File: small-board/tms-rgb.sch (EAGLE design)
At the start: 39 parts, among them J1 Pads, U1 CD74HC4053PWR, U100 TMS992XA, U2 TS5A4597DCKR, U3 LM1881MX/NOPB, U4 MAX4395EUD, U5 SN74LVC2G17DCKR, U6 LMH1251MT/NOPB, U7 THS7374IPWR

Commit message: Major layout rework for v2
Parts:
- removed C16: 100nF, tms-rgb:C0603
- C10: value 100nF -> 10uF; device tms-rgb:C0603 -> tms-rgb:C1206
- C11: value 10uF -> 100nF; device tms-rgb:C1206 -> tms-rgb:C0603
- R2: value 150 -> 910
- R3: value 220 -> 680
- R4: value 680 -> 220
- R6: value 910 -> 150
- U2: value TS5A4597DCKR -> LM1881MX/NOPB; device tms-rgb:TS5A4597DCKR -> tms-rgb:LM1881MX/NOPB
- U3: value LM1881MX/NOPB -> MAX4395EUD; device tms-rgb:LM1881MX/NOPB -> tms-rgb:MAX4395EUD
- U4: value MAX4395EUD -> TS5A4597DCKR; device tms-rgb:MAX4395EUD -> tms-rgb:TS5A4597DCKR
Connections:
- net B-Y: now also U1.Z1, U4.NC; no longer U1.Y1, U2.NC
- net CSYNC: now also U4.IN; no longer U2.IN
- net GND: now also C10.2, U3.VEE, U4.GND; no longer C16.2, C5.2, U3.GND, U4.VEE
- net N$1: now also R4.1, U3.A, U3.A-; no longer R3.1, U4.A, U4.A-
- net N$10: now also U1.Y, U3.C+; no longer U1.X, U4.C+
- net N$12: now also C9.1, R4.2, R7.2; no longer C7.1, R2.2, R3.2
- net N$13: now also C6.1, R2.2, R3.2; no longer C8.1, R4.2, R6.2
- net N$14: now also C5.1, C7.1, C8.1, R6.2; no longer C10.1, C6.1, C9.1, R7.2
- net N$2: now also R3.1, U3.B, U3.B-; no longer R4.1, U4.B, U4.B-
- net N$20: now also C5.2, U2.VIDEO_IN; no longer C6.2, U3.VIDEO_IN
- net N$21: now also C9.2; no longer C7.2
- net N$22: now also C6.2; no longer C8.2
- net N$23: now also C8.2; no longer C10.2
- net N$24: now also C7.2; no longer C9.2
- net N$3: now also U3.C, U3.C-; no longer U4.C, U4.C-
- net N$4: now also U3.D+, U4.COM; no longer U2.COM, U4.D+
- net N$5: now also U2.BURST; no longer U3.BURST
- net N$6: now also U2.CSYNC; no longer U3.CSYNC
- net N$7: now also U2.R_SET; no longer U3.R_SET
- net N$8: now also U1.X, U3.A+; no longer U1.Z, U4.A+
- net N$9: now also U1.Z, U3.B+; no longer U1.Y, U4.B+
- net R-Y: now also U1.X1; no longer U1.Z1
- net SAMPLE: now also U1.X0, U3.D, U3.D-; no longer U1.Y0, U4.D, U4.D-
- net VCC: now also C10.1; no longer C16.1, C5.1
- net Y: now also U1.Y0, U1.Y1; no longer U1.X0, U1.X1
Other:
- moved on the sheet: C1, C10, C11, C12, C13, C14, C15, C2, C3, C4, C5, C6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

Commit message: Named a few signals
And bridged a distant VCC fill
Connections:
- net N$10 renamed MX_Y
- net N$12 renamed SC_R
- net N$13 renamed SC_B
- net N$14 renamed SC_Y
- net N$4 renamed HOLD
- net N$8 renamed MX_R
- net N$9 renamed MX_B
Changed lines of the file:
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@@
 </segment>
 </net>
-<net name="N$8" class="0">
+<net name="MX_R" class="0">
 <segment>
 <pinref part="U1" gate="A" pin="X"/>
@@
 </segment>
 </net>
-<net name="N$9" class="0">
+<net name="MX_B" class="0">
 <segment>
 <pinref part="U1" gate="A" pin="Z"/>
@@
 </segment>
 </net>
-<net name="N$10" class="0">
+<net name="MX_Y" class="0">
 <segment>
 <pinref part="U1" gate="A" pin="Y"/>
@@
 </segment>
 </net>
-<net name="N$12" class="0">
+<net name="SC_R" class="0">
 <segment>
 <pinref part="R4" gate="G$1" pin="2"/>
@@
 </segment>
 </net>
-<net name="N$13" class="0">
+<net name="SC_B" class="0">
 <segment>
 <pinref part="R3" gate="G$1" pin="2"/>
@@
 </segment>
 </net>
-<net name="N$14" class="0">
+<net name="SC_Y" class="0">
 <segment>
 <pinref part="R5" gate="G$1" pin="2"/>
@@
 </segment>
 </net>
-<net name="N$4" class="0">
+<net name="HOLD" class="0">
 <segment>
 <pinref part="U3" gate="A" pin="D+"/>

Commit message: More than 100 improvements
Nearly all of which were suggested by MrPix from the AtariAge forums to improve the electrical characteristics of the board.
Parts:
- removed C15: 100nF, tms-rgb:C0603
- added FID1, FID2: FIDUCIAL, tms-rgb:FIDUCIAL
- C10: value 10uF -> 100nF; device tms-rgb:C1206 -> tms-rgb:C0603
- C3: value 100nF -> 10nF
- C4: value 10nF -> 100nF
- C9: value 100nF -> 10uF; device tms-rgb:C0603 -> tms-rgb:C1206
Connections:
- net GND: now also C14.2, C9.2; no longer C11.2, C15.2, C4.2
- net HOLD: now also C3.1; no longer C4.1
- net N$20: now also C4.2; no longer C5.2
- net N$21: now also C5.2; no longer C9.2
- net N$25: now also C11.1; no longer C12.1
- net N$26: now also C12.1; no longer C13.1
- net N$27: now also C13.1; no longer C14.1
- net N$28: now also C11.2; no longer C12.2
- net N$29: now also C12.2; no longer C13.2
- net N$30: now also C13.2; no longer C14.2
- net SC_R: now also C5.1, R6.2; no longer C9.1, R7.2
- net SC_Y: now also C4.1, R7.2; no longer C5.1, R6.2
- net VCC: now also C14.1, C9.1; no longer C11.1, C15.1, C3.1
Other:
- note added: "Nicholas Piegdon May 31, 2020 v2 CERN-OHL-W v2 github.com/npiegdon/tms-rgb nicholas.piegdon.info/tms-rgb @npiegdon"
- note removed: "Nicholas Piegdon May 17, 2020 v1+ CERN-OHL-W v2 github.com/npiegdon/tms-rgb nicholas.piegdon.info/tms-rgb @npiegdon"
- moved on the sheet: C10, C11, C12, C13, C14, C3, C4, C5, C9, R6, R7

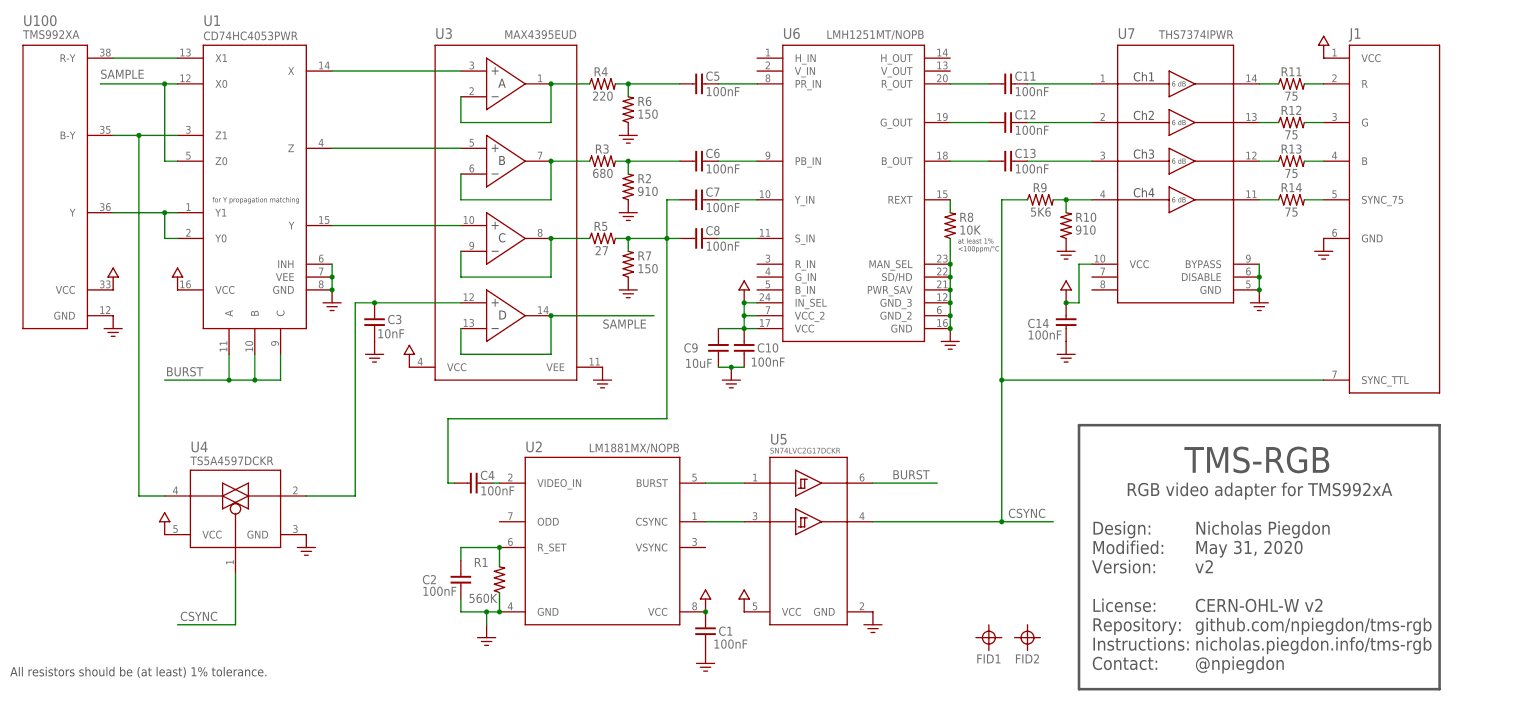
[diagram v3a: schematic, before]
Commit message: Updated voltage dividers
Now we consume around 15mA less with no discernible change to the image.
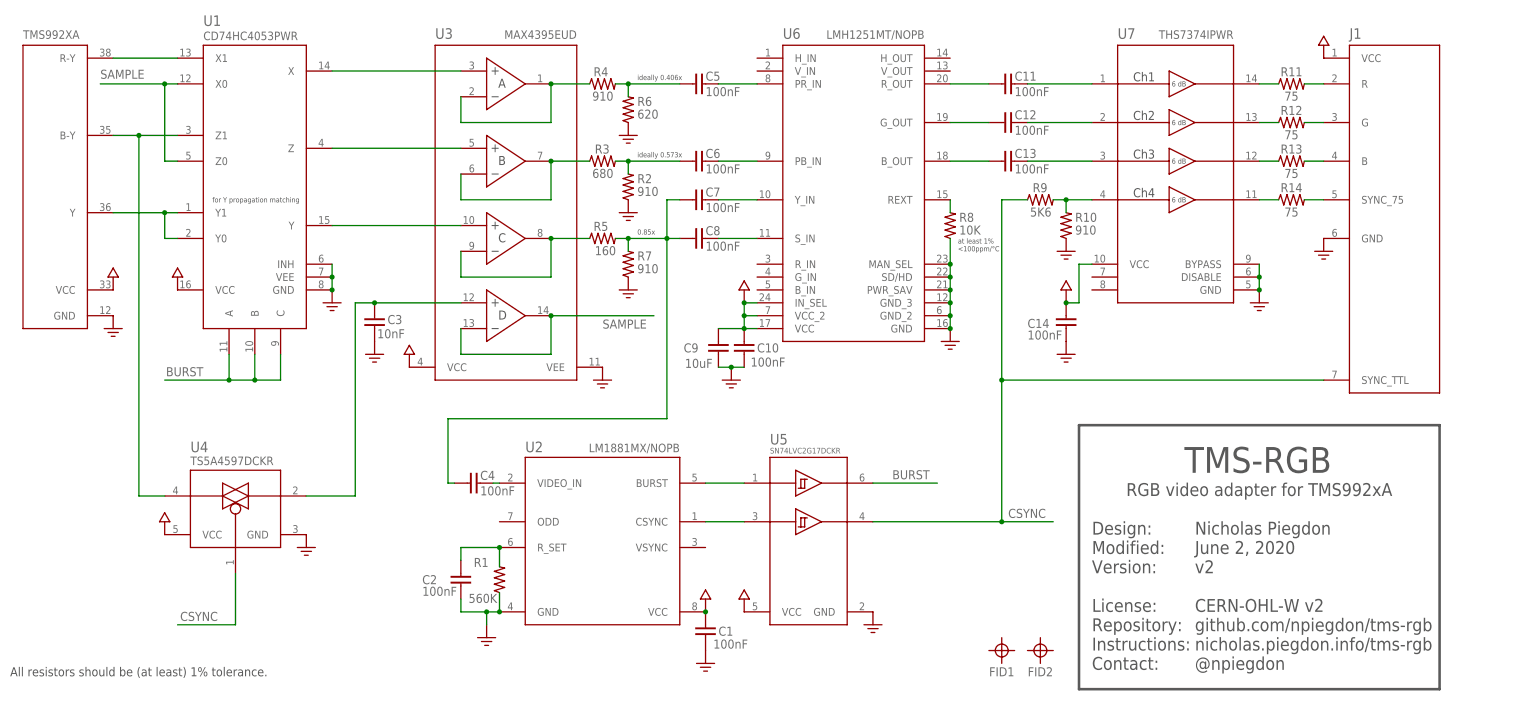
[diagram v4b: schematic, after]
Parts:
- R4: value 220 -> 910
- R5: value 27 -> 160
- R6: value 150 -> 620
- R7: value 150 -> 910
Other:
- note added: "0.85x"
- note added: "Nicholas Piegdon June 2, 2020 v2 CERN-OHL-W v2 github.com/npiegdon/tms-rgb nicholas.piegdon.info/tms-rgb @npiegdon"
- note added: "ideally 0.406x"
- note added: "ideally 0.573x"
- note removed: "Nicholas Piegdon May 31, 2020 v2 CERN-OHL-W v2 github.com/npiegdon/tms-rgb nicholas.piegdon.info/tms-rgb @npiegdon"
- moved on the sheet: FID1, FID2
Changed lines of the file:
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@@
 <part name="SUPPLY8" library="tms-rgb" deviceset="5V" device=""/>
 <part name="R8" library="tms-rgb" deviceset="R" device="0603" value="10K"/>
-<part name="R4" library="tms-rgb" deviceset="R" device="0603" value="220"/>
+<part name="R4" library="tms-rgb" deviceset="R" device="0603" value="910"/>
 <part name="R3" library="tms-rgb" deviceset="R" device="0603" value="680"/>
-<part name="R5" library="tms-rgb" deviceset="R" device="0603" value="27"/>
-<part name="R6" library="tms-rgb" deviceset="R" device="0603" value="150"/>
+<part name="R5" library="tms-rgb" deviceset="R" device="0603" value="160"/>
+<part name="R6" library="tms-rgb" deviceset="R" device="0603" value="620"/>
 <part name="R2" library="tms-rgb" deviceset="R" device="0603" value="910"/>
-<part name="R7" library="tms-rgb" deviceset="R" device="0603" value="150"/>
+<part name="R7" library="tms-rgb" deviceset="R" device="0603" value="910"/>
 <part name="GND9" library="tms-rgb" deviceset="GND" device=""/>
 <part name="GND10" library="tms-rgb" deviceset="GND" device=""/>
@@
 <plain>
 <text x="236.22" y="33.02" size="2.54" layer="97" align="top-left">Nicholas Piegdon
-May 31, 2020
+June 2, 2020
 v2
 CERN-OHL-W v2
@@
 <text x="2.54" y="2.54" size="1.778" layer="97">All resistors should be (at least) 1% tolerance.</text>
 <text x="42.418" y="96.012" size="1.016" layer="97">for Y propagation matching</text>
+<text x="126.238" y="120.142" size="1.016" layer="97">ideally 0.406x</text>
+<text x="126.238" y="104.902" size="1.016" layer="97">ideally 0.573x</text>
+<text x="126.238" y="89.662" size="1.016" layer="97">0.85x</text>
 </plain>
 <instances>
@@
 </instance>
 <instance part="U100" gate="A" x="5.08" y="127" smashed="yes">
-<attribute name="NAME" x="5.08" y="130.81" size="2.0828" layer="95" ratio="6" rot="SR0"/>
+<attribute name="NAME" x="5.08" y="130.81" size="2.0828" layer="95" ratio="6" rot="SR0" display="off"/>
 <attribute name="VALUE" x="5.08" y="128.27" size="1.6764" layer="96" ratio="6" rot="SR0"/>
 </instance>
@@
 <instance part="SUPPLY2" gate="G$1" x="147.32" y="15.24" smashed="yes"/>
 <instance part="GND14" gate="G$1" x="74.422" y="66.04" smashed="yes"/>
-<instance part="FID1" gate="G$1" x="195.58" y="10.16" smashed="yes">
-<attribute name="NAME" x="195.58" y="5.08" size="1.778" layer="95" align="bottom-center"/>
-</instance>
-<instance part="FID2" gate="G$1" x="203.2" y="10.16" smashed="yes">
-<attribute name="NAME" x="203.2" y="5.08" size="1.778" layer="95" align="bottom-center"/>
+<instance part="FID1" gate="G$1" x="198.12" y="7.62" smashed="yes">
+<attribute name="NAME" x="198.12" y="2.54" size="1.778" layer="95" align="bottom-center"/>
+</instance>
+<instance part="FID2" gate="G$1" x="205.74" y="7.62" smashed="yes">
+<attribute name="NAME" x="205.74" y="2.54" size="1.778" layer="95" align="bottom-center"/>
 </instance>
 </instances>

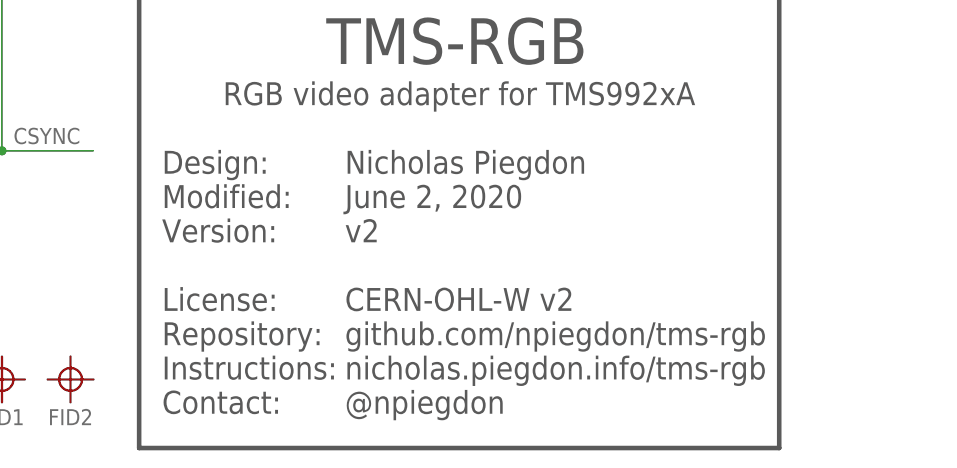
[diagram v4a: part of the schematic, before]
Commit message: Updated instructions URL
The new place is https://tms-rgb.com
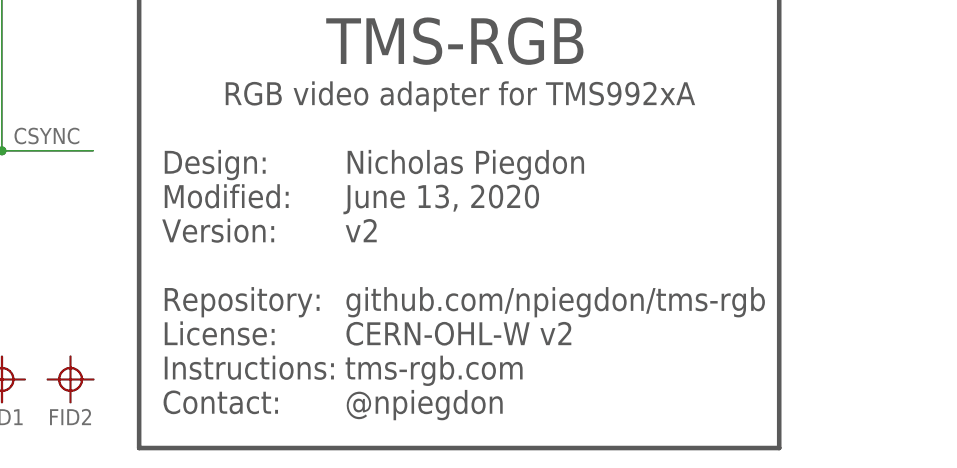
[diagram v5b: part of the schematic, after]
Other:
- note added: "Design: Modified: Version: Repository: License: Instructions: Contact:"
- note added: "Nicholas Piegdon June 13, 2020 v2 github.com/npiegdon/tms-rgb CERN-OHL-W v2 tms-rgb.com @npiegdon"
- note removed: "Design: Modified: Version: License: Repository: Instructions: Contact:"
- note removed: "Nicholas Piegdon June 2, 2020 v2 CERN-OHL-W v2 github.com/npiegdon/tms-rgb nicholas.piegdon.info/tms-rgb @npiegdon"
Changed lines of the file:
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@@
 <plain>
 <text x="236.22" y="33.02" size="2.54" layer="97" align="top-left">Nicholas Piegdon
-June 2, 2020
+June 13, 2020
 v2
+github.com/npiegdon/tms-rgb
 CERN-OHL-W v2
-github.com/npiegdon/tms-rgb
-nicholas.piegdon.info/tms-rgb
+tms-rgb.com
 @npiegdon</text>
 <text x="215.9" y="33.02" size="2.54" layer="97" align="top-left">Design:
 Modified:
 Version:
+Repository:
 License:
-Repository:
 Instructions:
 Contact:</text>
